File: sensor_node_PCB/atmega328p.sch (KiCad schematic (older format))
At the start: 14 parts, among them SW1 RESET_SWITCH, U5 ATMEGA328P, X2 CSTCE16MOV53-R0

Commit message: routing started 15%
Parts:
- removed R17: 1M, Resistor_SMD:R_0603_1608Metric, symbol Arduino_Uno_R3_From_Scratch-rescue:R
- removed X2: CSTCE16MOV53-R0, symbol Arduino_Uno_R3_From_Scratch-rescue:CERAMIC_RESONATOR
- added C7, C8: 18pF, Capacitor_SMD:C_0603_1608Metric, symbol Arduino_Uno_R3_From_Scratch-rescue:C
- added Y1: Crystal, Crystal:Crystal_SMD_5032-2Pin_5.0x3.2mm, symbol Arduino_Uno_R3_From_Scratch-rescue:Crystal
- D7: footprint (none) -> Diode_SMD:D_SOD-123
- ICSP2: footprint (none) -> Connector_PinHeader_2.54mm:PinHeader_2x03_P2.54mm_Vertical_SMD
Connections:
- net GND: now also C7.2, C8.2
- net at U5.10 (XTAL2): now also C7.1, Y1.1
- net at U5.9 (XTAL1): now also C8.1, Y1.2
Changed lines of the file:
@@
 	1    0    0    -1
 $EndComp
-Wire Wire Line
-	5650 2050 5650 2400
-Connection ~ 5650 2050
-Wire Wire Line
-	5650 2700 5650 3050
-Connection ~ 5650 3050
 Text HLabel 4800 3750 0    40   Input ~ 0
 AREF
@@
 F 0 "ICSP2" H 3800 1100 50  0000 C CNN
 F 1 "M20-9980346" H 3800 650 40  0000 C CNN
-F 2 "" H 3800 850 60  0001 C CNN
+F 2 "Connector_PinHeader_2.54mm:PinHeader_2x03_P2.54mm_Vertical_SMD" H 3800 850 60  0001 C CNN
 F 3 "http://cdn.harwin.com/pdfs/M20-998.pdf" H 3800 850 60  0001 C CNN
 F 4 "6 CONTACT(S), MALE, STRAIGHT TWO PART BOARD CONNECTOR" H 3800 850 60  0001 C CNN "Characteristics"
@@
 F 0 "D7" H 5300 1300 40  0000 C CNN
 F 1 "1N4148W-7-F" H 5300 1100 40  0000 C CNN
-F 2 "" H 5300 1200 60  0001 C CNN
+F 2 "Diode_SMD:D_SOD-123" H 5300 1200 60  0001 C CNN
 F 3 "http://www.diodes.com/_files/datasheets/ds30086.pdf" H 5300 1200 60  0001 C CNN
 F 4 "DIODE GEN PURP 100V 300MA SOD123" H 5300 1200 60  0001 C CNN "Characteristics"
@@
 	0    -1   -1   0
 $EndComp
-$Comp
-L Arduino_Uno_R3_From_Scratch-rescue:CERAMIC_RESONATOR X2
-U 1 1 5614A1DB
-P 5250 2550
-F 0 "X2" V 5325 2450 50  0000 R CNN
-F 1 "CSTCE16MOV53-R0" V 5175 2450 40  0000 R CNN
-F 2 "" H 5250 2550 60  0001 C CNN
-F 3 "http://www.murata.com/~/media/webrenewal/support/library/catalog/products/timingdevice/ceralock/p16e.ashx" H 5250 2550 60  0001 C CNN
-F 4 "CER RESONATOR 16.0MHZ SMD" H 5250 2550 60  0001 C CNN "Characteristics"
-F 5 "ATMEGA328P Oscillator" H 5250 2550 60  0001 C CNN "Description"
-F 6 "Murata" H 5250 2550 60  0001 C CNN "MFN"
-F 7 "CSTCE16M0V53-R0" H 5250 2550 60  0001 C CNN "MFP"
-F 8 "SMD" H 5250 2550 60  0001 C CNN "Package ID"
-F 9 "ANY" H 5250 2550 60  0001 C CNN "Source"
-F 10 "Y" H 5250 2550 60  0001 C CNN "Critical"
-F 11 "328P_Sub" H 5250 2550 60  0001 C CNN "Subsystem"
-F 12 "~" H 5250 2550 60  0001 C CNN "Notes"
-	1    5250 2550
-	0    1    1    0
-$EndComp
-Wire Wire Line
-	5300 2050 5650 2050
-Wire Wire Line
-	5300 2050 5300 2150
-Wire Wire Line
-	5300 2950 5300 3050
-Wire Wire Line
-	5300 3050 5650 3050
-Wire Wire Line
-	5050 2550 4750 2550
-Wire Wire Line
-	4750 2550 4750 2900
 Text Notes 6150 1050 0    40   ~ 0
 Atmel Appnote: AVR042 - AVR Hardware Design Considerations\nhttp://www.atmel.com/Images/Atmel-2521-AVR-Hardware-Design-Considerations_ApplicationNote_AVR042.pdf\n\nRefer to this for PCB layout information
@@
 	0    -1   -1   0
 $EndComp
-$Comp
-L Arduino_Uno_R3_From_Scratch-rescue:R R17
-U 1 1 5615BCD3
-P 5650 2550
-F 0 "R17" H 5725 2500 40  0000 L CNN
-F 1 "1M" V 5650 2550 40  0000 C CNN
-F 2 "Resistor_SMD:R_0603_1608Metric" V 5580 2550 30  0001 C CNN
-F 3 "http://www.vishay.com/docs/20035/dcrcwe3.pdf" H 5650 2550 30  0001 C CNN
-F 4 "RES SMD 1M OHM 1% 1/8W 0805" H 5650 2550 60  0001 C CNN "Characteristics"
-F 5 "ATMEGA328P Xtal 1M Feedback Resistor" H 5650 2550 60  0001 C CNN "Description"
-F 6 "Vishay" H 5650 2550 60  0001 C CNN "MFN"
-F 7 "CRCW08051M00FKEA" H 5650 2550 60  0001 C CNN "MFP"
-F 8 "SMD_0805" H 5650 2550 60  0001 C CNN "Package ID"
-F 9 "ANY" H 5650 2550 60  0001 C CNN "Source"
-F 10 "N" H 5650 2550 60  0001 C CNN "Critical"
-F 11 "328P_Sub" H 5650 2550 60  0001 C CNN "Subsystem"
-F 12 "~" H 5650 2550 60  0001 C CNN "Notes"
-	1    5650 2550
-	1    0    0    -1
-$EndComp
 Wire Wire Line
 	3500 1650 3500 1775
@@
 L Arduino_Uno_R3_From_Scratch-rescue:GND #PWR044
 U 1 1 56207870
-P 4750 2900
-F 0 "#PWR044" H 4750 2900 30  0001 C CNN
-F 1 "GND" H 4750 2830 30  0001 C CNN
-F 2 "~" H 4750 2900 60  0000 C CNN
-F 3 "~" H 4750 2900 60  0000 C CNN
-F 4 "ANY" H 4750 2900 60  0001 C CNN "Source"
-F 5 "N" H 4750 2900 60  0001 C CNN "Critical"
-F 6 "~" H 4750 2900 60  0001 C CNN "Notes"
-	1    4750 2900
+P 4450 2525
+F 0 "#PWR044" H 4450 2525 30  0001 C CNN
+F 1 "GND" H 4450 2455 30  0001 C CNN
+F 2 "~" H 4450 2525 60  0000 C CNN
+F 3 "~" H 4450 2525 60  0000 C CNN
+F 4 "ANY" H 4450 2525 60  0001 C CNN "Source"
+F 5 "N" H 4450 2525 60  0001 C CNN "Critical"
+F 6 "~" H 4450 2525 60  0001 C CNN "Notes"
+	1    4450 2525
 	1    0    0    -1
 $EndComp
@@
 $EndComp
 Wire Wire Line
-	5650 2050 5850 2050
-Wire Wire Line
-	5650 3050 5850 3050
-Wire Wire Line
 	5600 4500 5600 4700
 Wire Wire Line
@@
 Wire Wire Line
 	5650 1500 5850 1500
+Wire Wire Line
+	5300 3050 5850 3050
+Wire Wire Line
+	5300 2050 5850 2050
+$Comp
+L Arduino_Uno_R3_From_Scratch-rescue:Crystal Y1
+U 1 1 5F569D4C
+P 5300 2575
+F 0 "Y1" V 5254 2706 50  0000 L CNN
+F 1 "Crystal" V 5345 2706 50  0000 L CNN
+F 2 "Crystal:Crystal_SMD_5032-2Pin_5.0x3.2mm" H 5300 2575 60  0001 C CNN
+F 3 "" H 5300 2575 60  0000 C CNN
+	1    5300 2575
+	0    1    1    0
+$EndComp
+Wire Wire Line
+	5300 2050 5300 2425
+Wire Wire Line
+	5300 2725 5300 3050
+$Comp
+L Arduino_Uno_R3_From_Scratch-rescue:C C7
+U 1 1 5F570541
+P 5000 2050
+F 0 "C7" V 4748 2050 50  0000 C CNN
+F 1 "18pF" V 4839 2050 50  0000 C CNN
+F 2 "Capacitor_SMD:C_0603_1608Metric" H 5038 1900 30  0001 C CNN
+F 3 "" H 5000 2050 60  0000 C CNN
+	1    5000 2050
+	0    1    1    0
+$EndComp
+$Comp
+L Arduino_Uno_R3_From_Scratch-rescue:C C8
+U 1 1 5F570D63
+P 5025 3050
+F 0 "C8" V 4773 3050 50  0000 C CNN
+F 1 "18pF" V 4864 3050 50  0000 C CNN
+F 2 "Capacitor_SMD:C_0603_1608Metric" H 5063 2900 30  0001 C CNN
+F 3 "" H 5025 3050 60  0000 C CNN
+	1    5025 3050
+	0    1    1    0
+$EndComp
+Wire Wire Line
+	5150 2050 5300 2050
+Connection ~ 5300 2050
+Wire Wire Line
+	5175 3050 5300 3050
+Connection ~ 5300 3050
+Wire Wire Line
+	4850 2050 4450 2050
+Wire Wire Line
+	4450 2050 4450 2400
+Wire Wire Line
+	4875 3050 4875 2400
+Wire Wire Line
+	4875 2400 4450 2400
+Connection ~ 4450 2400
+Wire Wire Line
+	4450 2400 4450 2525
 $EndSCHEMATC

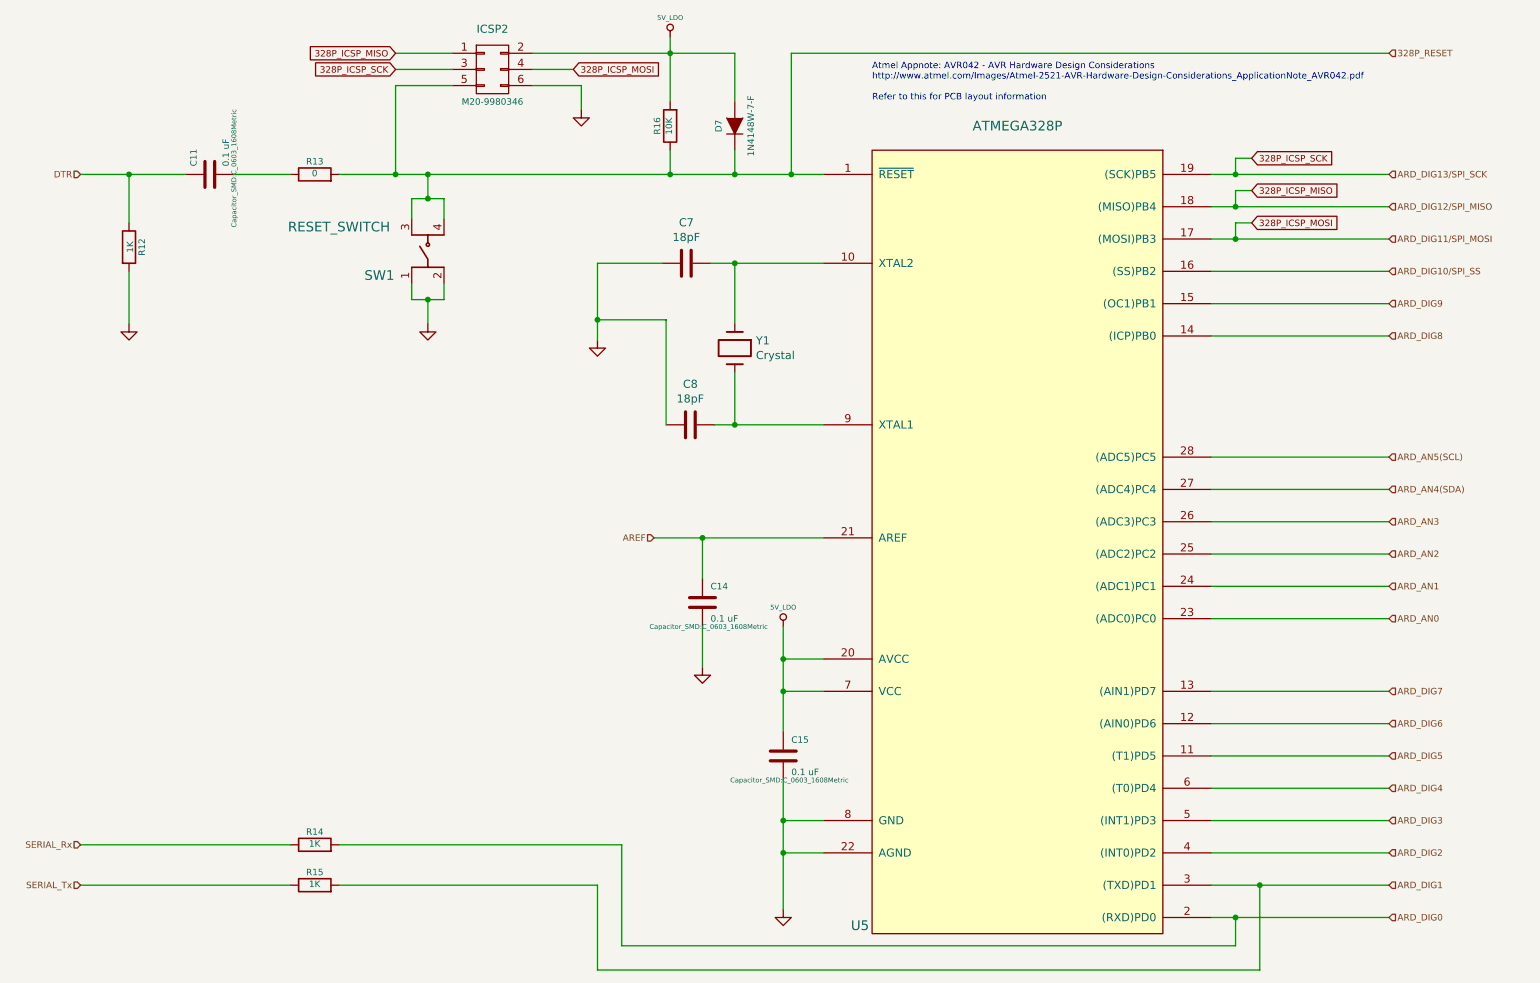
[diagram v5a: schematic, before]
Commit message: fixed incorrect atmega328p pinout
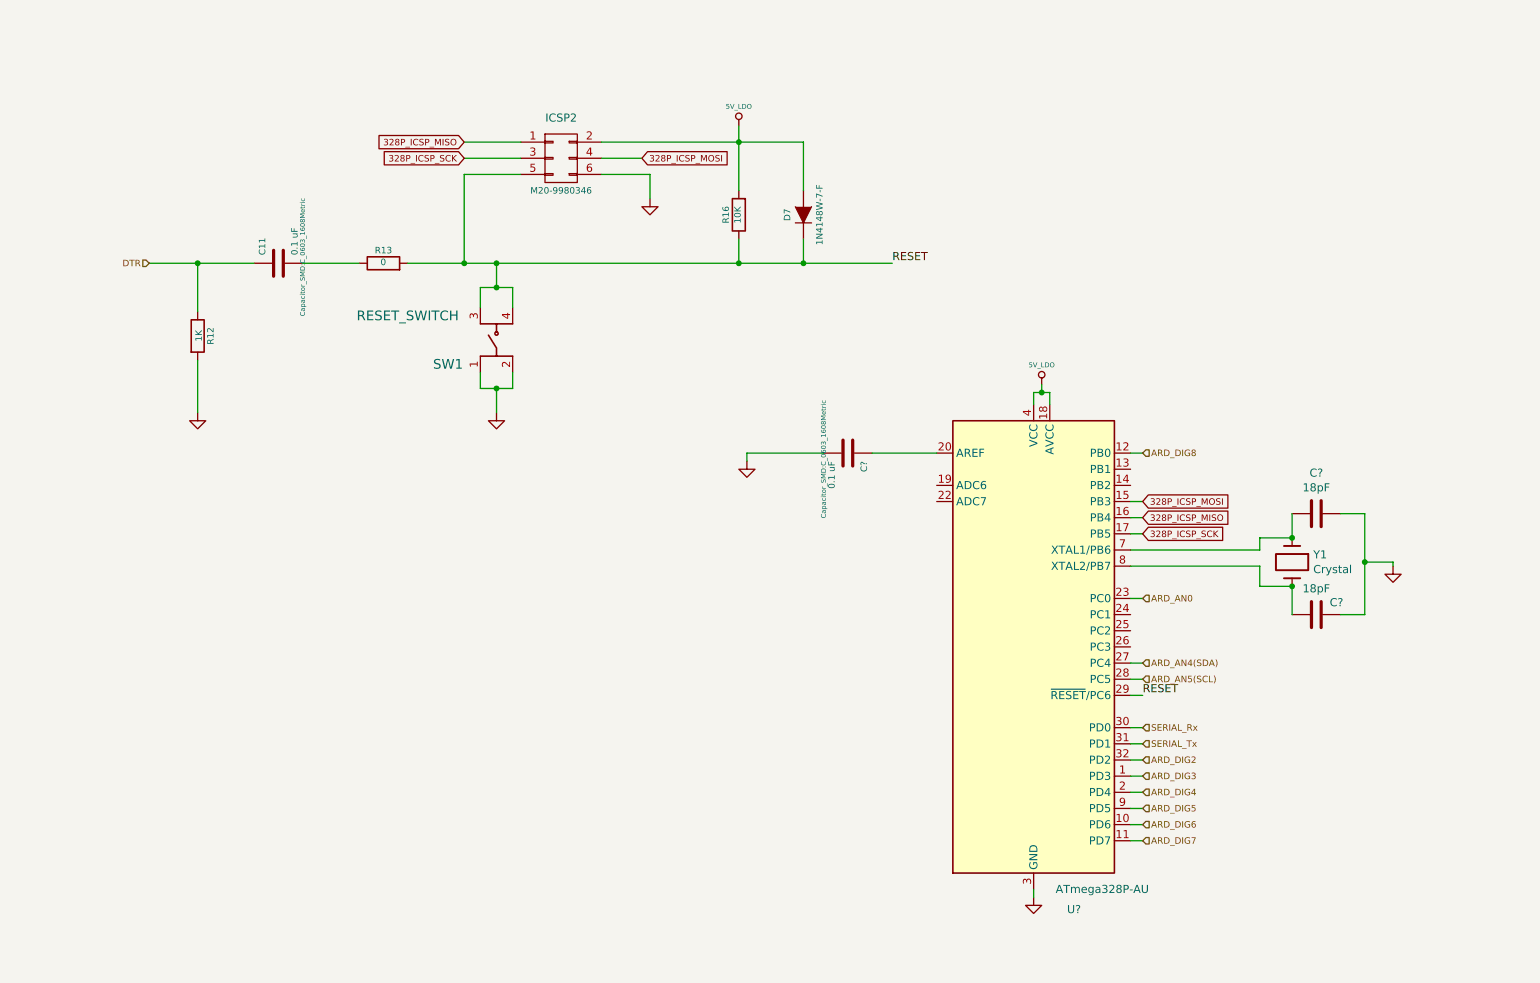
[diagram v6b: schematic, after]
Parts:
- removed C14, C15: 0.1 uF, Capacitor_SMD:C_0603_1608Metric, symbol Arduino_Uno_R3_From_Scratch-rescue:C
- removed C7, C8: 18pF, Capacitor_SMD:C_0603_1608Metric, symbol Arduino_Uno_R3_From_Scratch-rescue:C
- removed R14, R15: 1K, Resistor_SMD:R_0603_1608Metric, symbol Arduino_Uno_R3_From_Scratch-rescue:R
- removed U5: ATMEGA328P, Package_QFP:TQFP-32_7x7mm_P0.8mm, symbol Arduino_Uno_R3_From_Scratch-rescue:ATMEGA328P-PU
- added C? (x2): 18pF, Capacitor_SMD:C_0603_1608Metric, symbol Arduino_Uno_R3_From_Scratch-rescue:C
- added C?: 0.1 uF, Capacitor_SMD:C_0603_1608Metric, symbol Arduino_Uno_R3_From_Scratch-rescue:C
- added U?: ATmega328P-AU, Package_QFP:TQFP-32_7x7mm_P0.8mm, symbol MCU_Microchip_ATmega:ATmega328P-AU
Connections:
- net 328P_ICSP_MISO: now also U?.16 (PB4)
- net 328P_ICSP_MOSI: now also U?.15 (PB3)
- net 328P_ICSP_SCK: now also U?.17 (PB5)
- net 5V_LDO: now also U?.18 (AVCC), U?.4 (VCC), U?.6 (VCC)
- net ARD_AN0: now also U?.23 (PC0)
- net ARD_AN4(SDA): now also U?.27 (PC4)
- net ARD_AN5(SCL): now also U?.28 (PC5)
- net ARD_DIG2: now also U?.32 (PD2)
- net ARD_DIG3: now also U?.1 (PD3)
- net ARD_DIG4: now also U?.2 (PD4)
- net ARD_DIG5: now also U?.9 (PD5)
- net ARD_DIG6: now also U?.10 (PD6)
- net ARD_DIG7: now also U?.11 (PD7)
- net ARD_DIG8: now also U?.12 (PB0)
- net GND: now also C?.1, C?.1, C?.2, U?.21 (GND), U?.3 (GND), U?.5 (GND)
- net SERIAL_Rx: now also U?.30 (PD0)
- net SERIAL_Tx: now also U?.31 (PD1)
- net at Y1.1: now also C?.2, U?.7 (XTAL1/PB6)
- net at Y1.2: now also C?.2, U?.8 (XTAL2/PB7)
- net 328P_RESET renamed RESET
- net RESET: now also U?.29 (~RESET~/PC6)
- new net: C?.1, U?.20 (AREF)
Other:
- note removed: "Atmel Appnote: AVR042 - AVR Hardware Design Considerations\nhttp://www.atmel.com/Images/Atmel-2521-AVR-Hardware-Design-Considerations_ApplicationNote_AVR042.pdf\n\nRefer to this for PCB layout information"
- moved on the sheet: C11, D7, ICSP2, R12, R13, R16, SW1, Y1

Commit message: removed 2nd connector - fixed mounting holes
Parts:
- gave numbers to parts that had none: 4
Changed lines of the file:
@@
 $EndComp
 $Comp
-L MCU_Microchip_ATmega:ATmega328P-AU U?
+L MCU_Microchip_ATmega:ATmega328P-AU U5
 U 1 1 5F6ABACB
 P 7150 4425
-F 0 "U?" H 7400 2800 50  0000 C CNN
+F 0 "U5" H 7400 2800 50  0000 C CNN
 F 1 "ATmega328P-AU" H 7575 2925 50  0000 C CNN
 F 2 "Package_QFP:TQFP-32_7x7mm_P0.8mm" H 7150 4425 50  0001 C CIN
@@
 $EndComp
 $Comp
-L Arduino_Uno_R3_From_Scratch-rescue:C C?
+L Arduino_Uno_R3_From_Scratch-rescue:C C8
 U 1 1 5F6C2143
 P 8900 3600
-F 0 "C?" V 8648 3600 50  0000 C CNN
+F 0 "C8" V 8648 3600 50  0000 C CNN
 F 1 "18pF" V 8739 3600 50  0000 C CNN
 F 2 "Capacitor_SMD:C_0603_1608Metric" H 8938 3450 30  0001 C CNN
@@
 $EndComp
 $Comp
-L Arduino_Uno_R3_From_Scratch-rescue:C C?
+L Arduino_Uno_R3_From_Scratch-rescue:C C9
 U 1 1 5F6C2B63
 P 8900 4225
-F 0 "C?" V 8825 4350 50  0000 C CNN
+F 0 "C9" V 8825 4350 50  0000 C CNN
 F 1 "18pF" V 8739 4225 50  0000 C CNN
 F 2 "Capacitor_SMD:C_0603_1608Metric" H 8938 4075 30  0001 C CNN
@@
 Connection ~ 8750 4050
 $Comp
-L Arduino_Uno_R3_From_Scratch-rescue:GND #PWR?
+L Arduino_Uno_R3_From_Scratch-rescue:GND #PWR0139
 U 1 1 5F6CFD3D
 P 9375 3925
-F 0 "#PWR?" H 9375 3925 30  0001 C CNN
+F 0 "#PWR0139" H 9375 3925 30  0001 C CNN
 F 1 "GND" H 9375 3855 30  0001 C CNN
 F 2 "~" H 9375 3925 60  0000 C CNN
@@
 	9200 3900 9200 3600
 $Comp
-L Arduino_Uno_R3_From_Scratch-rescue:C C?
+L Arduino_Uno_R3_From_Scratch-rescue:C C7
 U 1 1 5F6D7CAF
 P 6000 3225
-F 0 "C?" H 6050 3325 40  0000 L CNN
+F 0 "C7" H 6050 3325 40  0000 L CNN
 F 1 "0.1 uF" H 6050 3125 40  0000 L CNN
 F 2 "Capacitor_SMD:C_0603_1608Metric" H 6038 3075 30  0000 C CNN
@@
 $EndComp
 $Comp
-L Arduino_Uno_R3_From_Scratch-rescue:GND #PWR?
+L Arduino_Uno_R3_From_Scratch-rescue:GND #PWR0140
 U 1 1 5F6DA776
 P 5375 3275
-F 0 "#PWR?" H 5375 3275 30  0001 C CNN
+F 0 "#PWR0140" H 5375 3275 30  0001 C CNN
 F 1 "GND" H 5375 3205 30  0001 C CNN
 F 2 "~" H 5375 3275 60  0000 C CNN
@@
 	7250 2850 7250 2925
 $Comp
-L Arduino_Uno_R3_From_Scratch-rescue:5V_LDO #PWR?
+L Arduino_Uno_R3_From_Scratch-rescue:5V_LDO #PWR0141
 U 1 1 5F6E82FA
 P 7200 2800
-F 0 "#PWR?" H 7200 2890 20  0001 C CNN
+F 0 "#PWR0141" H 7200 2890 20  0001 C CNN
 F 1 "5V_LDO" H 7200 2920 30  0000 C CNN
 F 2 "~" H 7200 2800 60  0000 C CNN
@@
 	7200 2850 7250 2850
 $Comp
-L Arduino_Uno_R3_From_Scratch-rescue:GND #PWR?
+L Arduino_Uno_R3_From_Scratch-rescue:GND #PWR0142
 U 1 1 5F6F085B
 P 7150 5975
-F 0 "#PWR?" H 7150 5975 30  0001 C CNN
+F 0 "#PWR0142" H 7150 5975 30  0001 C CNN
 F 1 "GND" H 7150 5905 30  0001 C CNN
 F 2 "~" H 7150 5975 60  0000 C CNN

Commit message: fixed max485 wiring issues on schematic
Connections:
- net ARD_DIG9: now reaches U5.13 (PB1)
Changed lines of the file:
@@
 Wire Wire Line
 	5725 2050 6275 2050
+Text HLabel 7825 3325 2    50   Input ~ 0
+ARD_DIG9
+Wire Wire Line
+	7750 3325 7825 3325
 $EndSCHEMATC
